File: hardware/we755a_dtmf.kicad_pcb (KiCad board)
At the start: 2 copper layers, 50.8 x 88.9 mm, 44 parts, among them J1 Conn_01x06_Male, J2 UPDI, J3 Conn_02x10_Odd_Even, U1 AVR128DA28-I/SS, U2 MT8870, U3 H11AA1, U4 LAA108, U5 LAA108, U6 LAA108, U7 LAA108, U8 LAA108, Y1 32.767KHz, Y2 3.579545MHZ

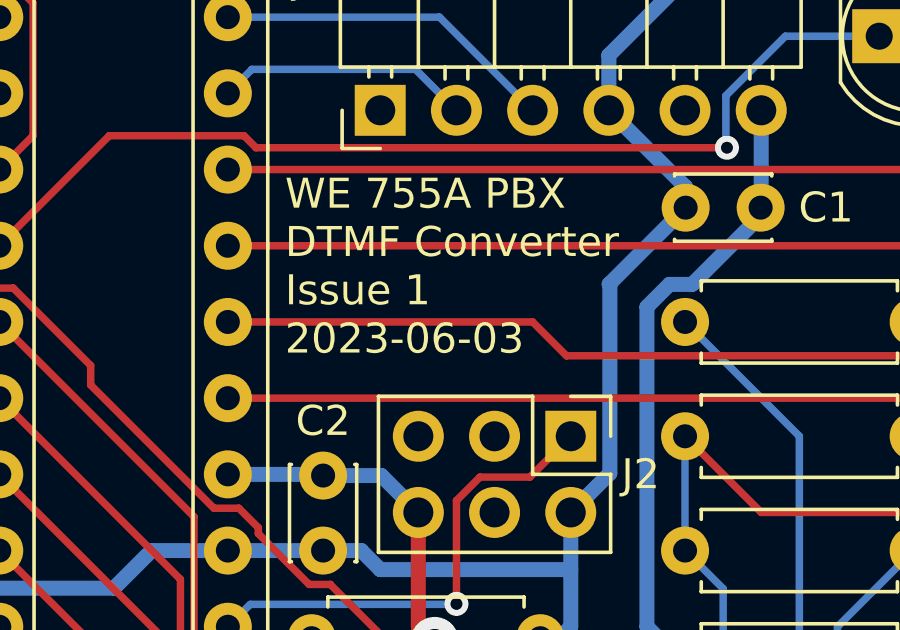
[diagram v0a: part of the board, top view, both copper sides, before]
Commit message: Update PCB to Rev2: No functional changes.
    * Rev 1 and Rev 2 PCBs are identical except for the silkscreen.
    * Rename LINK_B to LINK_E on schematic and layout.
    * Correct value of C1 on schematic.
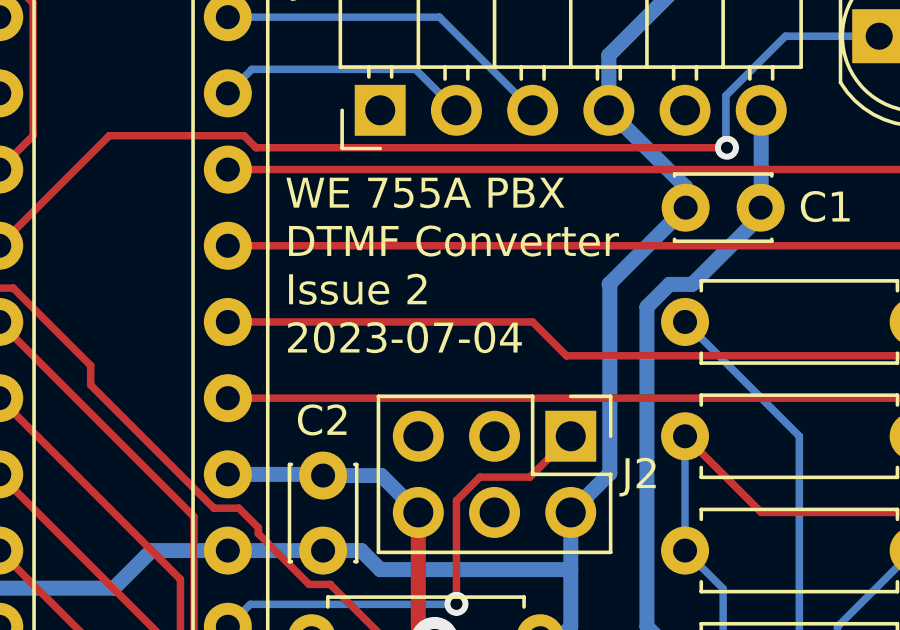
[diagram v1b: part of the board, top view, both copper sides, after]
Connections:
- net /LINK_B renamed /LINK_E
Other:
- board text added: "E"
- board text added: "WE 755A PBX DTMF Converter Issue 2 2023-07-04"
- board text added: "WE 755A PBX DTMF Converter github.com/hharte/we755a_dtmf Issue 2 - 2023-07-04"
- board text removed: "B"
- board text removed: "WE 755A PBX DTMF Converter Issue 1 2023-06-03"
- board text removed: "WE 755A PBX DTMF Converter github.com/hharte/we755a_dtmf Issue 1 - 2023-06-03"
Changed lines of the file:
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@@
   (title_block
     (title "WE 755A PBX DTMF Converter")
-    (date "2023-06-03")
-    (rev "1")
+    (date "2023-07-04")
+    (rev "2")
     (company "Howard M. Harte")
     (comment 1 "https://github.com/hharte/we755a_dtmf")
@@
   (net 24 "/WE755A_B0")
   (net 25 "GNDPWR")
-  (net 26 "/LINK_B")
+  (net 26 "/LINK_E")
   (net 27 "/LINK_T2")
   (net 28 "/LINK_T3")
@@
       (net 49 "Net-(R13-Pad2)") (pintype "passive"))
     (pad "2" thru_hole oval (at 0 2.54 270) (size 1.6 1.6) (drill 0.8) (layers "*.Cu" "*.Mask")
-      (net 26 "/LINK_B") (pintype "passive"))
+      (net 26 "/LINK_E") (pintype "passive"))
     (pad "3" thru_hole oval (at 0 5.08 270) (size 1.6 1.6) (drill 0.8) (layers "*.Cu" "*.Mask")
       (net 63 "unconnected-(U3-NC-Pad3)") (pinfunction "NC") (pintype "no_connect"))
@@
       (net 82 "unconnected-(J3-Pin_15-Pad15)") (pinfunction "Pin_15") (pintype "passive+no_connect"))
     (pad "16" thru_hole oval (at 2.54 17.78 270) (size 1.7 1.7) (drill 1) (layers "*.Cu" "*.Mask")
-      (net 26 "/LINK_B") (pinfunction "Pin_16") (pintype "passive"))
+      (net 26 "/LINK_E") (pinfunction "Pin_16") (pintype "passive"))
     (pad "17" thru_hole oval (at 0 20.32 270) (size 1.7 1.7) (drill 1) (layers "*.Cu" "*.Mask")
       (net 3 "/TIP") (pinfunction "Pin_17") (pintype "passive"))
@@
         (effects (font (size 1 1) (thickness 0.15)))
     )
-    (fp_text value "MountingHole" (at 0 3.7) (layer "F.Fab")
+    (fp_text value "MountingHole" (at 0 3.7) (layer "F.Fab") hide
         (effects (font (size 1 1) (thickness 0.15)))
     )
@@
     (effects (font (size 1 1) (thickness 0.15)) (justify left bottom mirror))
   )
-  (gr_text "WE 755A PBX DTMF Converter\ngithub.com/hharte/we755a_dtmf\nIssue 1 - 2023-06-03" (at 70.993 27.813) (layer "B.SilkS")
+  (gr_text "WE 755A PBX DTMF Converter\ngithub.com/hharte/we755a_dtmf\nIssue 2 - 2023-07-04" (at 70.993 27.813) (layer "B.SilkS")
     (effects (font (size 1 1) (thickness 0.15)) (justify left bottom mirror))
   )
-  (gr_text "B" (at 53.721 110.744) (layer "B.SilkS")
+  (gr_text "E" (at 53.721 110.744) (layer "B.SilkS")
     (effects (font (size 1 1) (thickness 0.15)) (justify left bottom mirror))
   )
@@
     (effects (font (size 1 1) (thickness 0.15)) (justify left bottom))
   )
-  (gr_text "WE 755A PBX\nDTMF Converter\nIssue 1\n2023-06-03" (at 47.625 41.783) (layer "F.SilkS")
+  (gr_text "WE 755A PBX\nDTMF Converter\nIssue 2\n2023-07-04" (at 47.625 41.783) (layer "F.SilkS")
     (effects (font (size 1 1) (thickness 0.15)) (justify left bottom))
   )
   (dimension (type aligned) (layer "Dwgs.User")
+    (pts (xy 36.195 108.585) (xy 36.195 111.76))
+    (height 5.461)
+    (gr_text "3.1750 mm" (at 30.6324 116.5352 90) (layer "Dwgs.User")
+      (effects (font (size 1 1) (thickness 0.15)))
+    )
+    (format (prefix "") (suffix "") (units 3) (units_format 1) (precision 4))
+    (style (thickness 0.12) (arrow_length 1.27) (text_position_mode 2) (extension_height 0.58642) (extension_offset 0.5) keep_text_aligned)
+  )
+  (dimension (type aligned) (layer "Dwgs.User")
+    (pts (xy 36.195 108.585) (xy 80.645 108.585))
+    (height 8.763)
+    (gr_text "44.4500 mm" (at 58.42 116.198) (layer "Dwgs.User")
+      (effects (font (size 1 1) (thickness 0.15)))
+    )
+    (format (prefix "") (suffix "") (units 3) (units_format 1) (precision 4))
+    (style (thickness 0.12) (arrow_length 1.27) (text_position_mode 0) (extension_height 0.58642) (extension_offset 0.5) keep_text_aligned)
+  )
+  (dimension (type aligned) (layer "Dwgs.User")
     (pts (xy 32.385 22.86) (xy 32.385 111.76))
-    (height 1.905)
-    (gr_text "88.9000 mm" (at 29.33 67.31 90) (layer "Dwgs.User")
+    (height 5.1054)
+    (gr_text "88.9000 mm" (at 28.194 67.31 90) (layer "Dwgs.User")
       (effects (font (size 1 1) (thickness 0.15)))
     )
     (format (prefix "") (suffix "") (units 2) (units_format 1) (precision 4))
-    (style (thickness 0.15) (arrow_length 1.27) (text_position_mode 0) (extension_height 0.58642) (extension_offset 0) keep_text_aligned)
+    (style (thickness 0.15) (arrow_length 1.27) (text_position_mode 2) (extension_height 0.58642) (extension_offset 0) keep_text_aligned)
   )
   (dimension (type aligned) (layer "Dwgs.User")
@@
     (style (thickness 0.15) (arrow_length 1.27) (text_position_mode 0) (extension_height 0.58642) (extension_offset 0) keep_text_aligned)
   )
+  (dimension (type aligned) (layer "Dwgs.User")
+    (pts (xy 36.195 108.585) (xy 33.02 108.585))
+    (height -6.8326)
+    (gr_text "3.1750 mm" (at 41.0464 115.5192) (layer "Dwgs.User")
+      (effects (font (size 1 1) (thickness 0.15)))
+    )
+    (format (prefix "") (suffix "") (units 3) (units_format 1) (precision 4))
+    (style (thickness 0.12) (arrow_length 1.27) (text_position_mode 2) (extension_height 0.58642) (extension_offset 0.5) keep_text_aligned)
+  )
   (segment (start 45.4828 76.4772) (end 50.8 71.16) (width 0.5) (layer "F.Cu") (net 1))

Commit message: Update to KiCAD 8.0.1.
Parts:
- C1: value 1uF -> 0.1uF

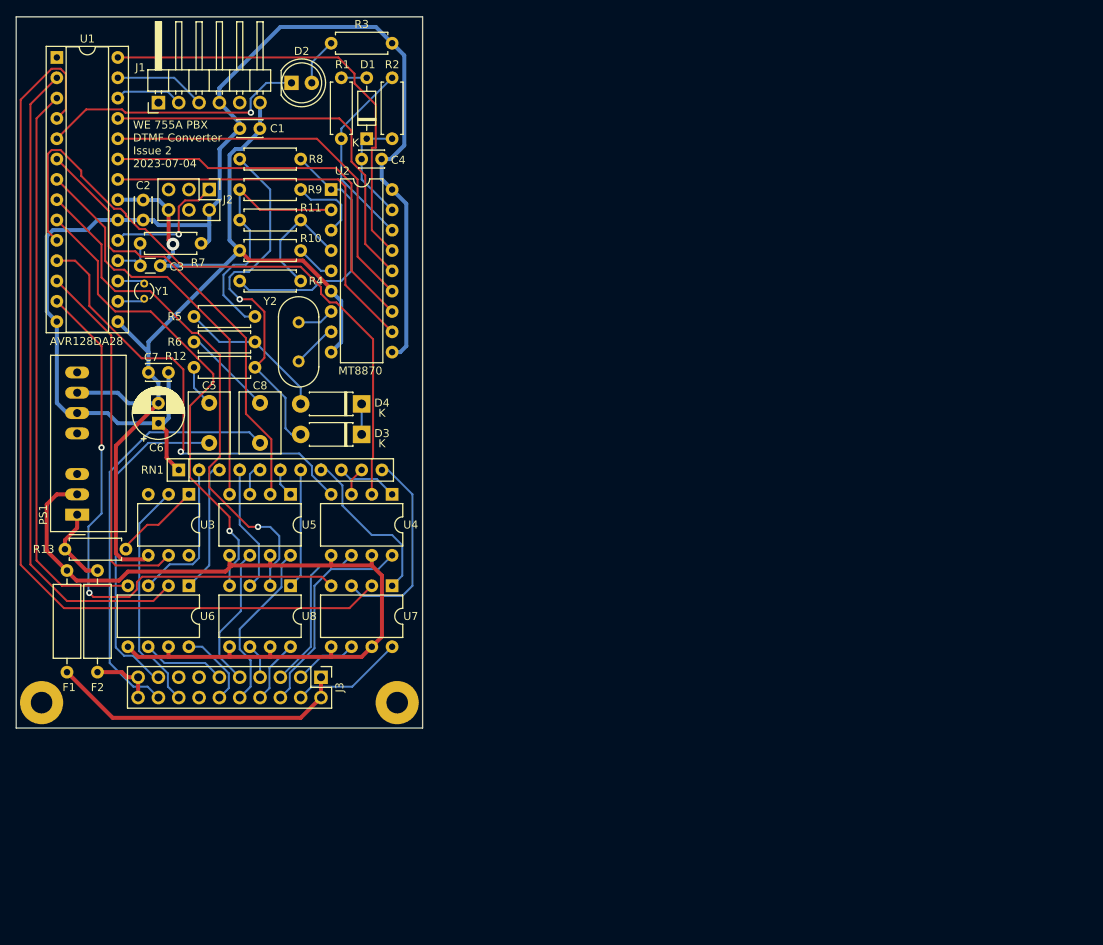
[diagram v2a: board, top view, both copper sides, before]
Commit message: Issue 3: Smaller board.     * Smaller board.     * Jumper options for DTMF converter and station concentrator.
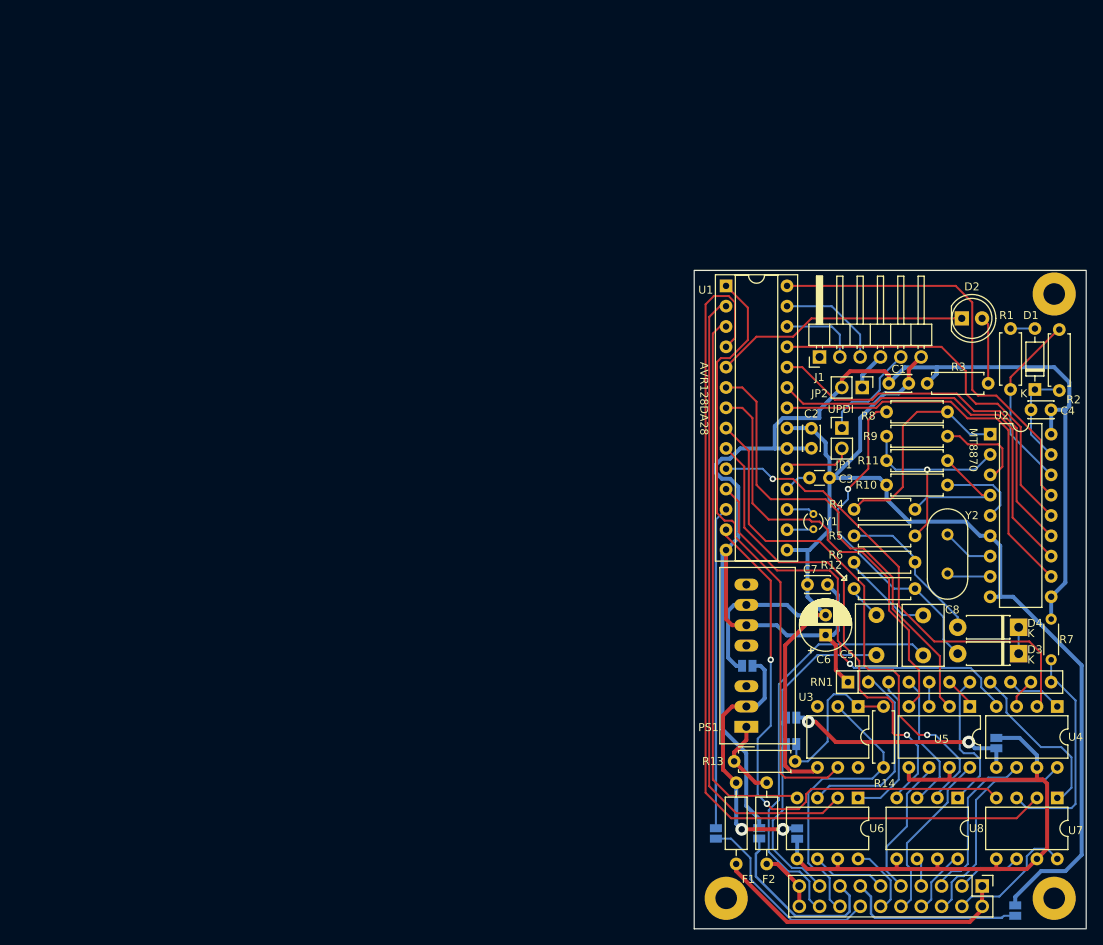
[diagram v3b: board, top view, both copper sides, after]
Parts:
- removed H1, H2: MountingHole, MountingHole:MountingHole_2.7mm_Pad
- removed J2: UPDI, Connector_PinHeader_2.54mm:PinHeader_2x03_P2.54mm_Vertical
- added JP1: Jumper_2_Open, Connector_PinHeader_2.54mm:PinHeader_1x02_P2.54mm_Vertical, F.Cu at (136.2, 74.3)
- added JP10: 5V_J3, Jumper:SolderJumper-2_P1.3mm_Open_Pad1.0x1.5mm, B.Cu at (120.5, 124.9)
- added JP2: Jumper_2_Open, Connector_PinHeader_2.54mm:PinHeader_1x02_P2.54mm_Vertical, F.Cu at (138.8, 69.2)
- added JP3: GRD_TIE, Jumper:SolderJumper-2_P1.3mm_Open_Pad1.0x1.5mm, B.Cu at (124.4, 104.0)
- added JP4: LINK6_G_SSR, Jumper:SolderJumper-2_P1.3mm_Open_Pad1.0x1.5mm, B.Cu at (155.5, 113.6)
- added JP5: G_SSR_GNDPWR, Jumper:SolderJumper-2_P1.3mm_Open_Pad1.0x1.5mm, B.Cu at (130.6, 125.0)
- added JP6: TIP_IN, Jumper:SolderJumper-2_P1.3mm_Open_Pad1.0x1.5mm, B.Cu at (129.9, 113.8)
- added JP7: LINK6_TIP, Jumper:SolderJumper-2_P1.3mm_Open_Pad1.0x1.5mm, B.Cu at (129.9, 110.5)
- added JP8: GND_J3, Jumper:SolderJumper-2_P1.3mm_Open_Pad1.0x1.5mm, B.Cu at (157.9, 134.6)
- added JP9: 5V_J3, Jumper:SolderJumper-2_P1.3mm_Open_Pad1.0x1.5mm, B.Cu at (125.9, 124.9)
- added R14: 120, Resistor_THT:R_Axial_DIN0207_L6.3mm_D2.5mm_P7.62mm_Horizontal, F.Cu at (141.4, 116.7)
- F1, F2: footprint Resistor_THT:R_Axial_DIN0309_L9.0mm_D3.2mm_P12.70mm_Horizontal -> Resistor_THT:R_Axial_DIN0207_L6.3mm_D2.5mm_P10.16mm_Horizontal
- J3: footprint Connector_PinHeader_2.54mm:PinHeader_2x10_P2.54mm_Vertical -> ac125a_dtmf:WE755A-DTMF
- PS1: value SPBW06 -> SPBW06-5
- R7: value 4.7K -> 220; footprint Resistor_THT:R_Axial_DIN0207_L6.3mm_D2.5mm_P7.62mm_Horizontal -> Resistor_THT:R_Axial_DIN0204_L3.6mm_D1.6mm_P5.08mm_Horizontal
- RN1: value R_Network10_US -> R_Network10_220R
- moved R7 116.2 mm to (162.4, 98.1), turned to -90 degrees
- moved R3 92.5 mm to (154.5, 68.7), turned to 180 degrees
- moved C4 89.3 mm to (159.9, 72.0)
- moved R1 89.3 mm to (157.3, 61.8)
- moved D1 89.2 mm to (160.4, 69.4)
- moved R2 89.1 mm to (163.4, 69.6)
- moved U5 89.0 mm to (152.2, 109.1)
- moved D2 88.8 mm to (151.2, 60.6)
- moved J1 88.5 mm to (133.4, 65.4)
- moved Y1 88.5 mm to (132.7, 85.0)
- moved U1 88.4 mm to (121.8, 56.5)
- moved C2 88.3 mm to (132.4, 76.8)
- moved U2 87.9 mm to (154.8, 75.0)
- moved RN1 87.8 mm to (137.0, 106.0)
- moved R13 87.8 mm to (122.8, 115.9)
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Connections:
- J1 pad 4: +5V -> Net-(J1-Pin_4)
- J1 pad 5: unconnected-(J1-Pin_5-Pad5) -> /UPDI_EXT
- J3 pad 13: unconnected-(J3-Pin_13-Pad13) -> /GND_J3
- J3 pad 14: unconnected-(J3-Pin_14-Pad14) -> /PD6_J3
- J3 pad 15: unconnected-(J3-Pin_15-Pad15) -> /5V_J3
- R7 pad 2: /RESET# -> Net-(RN1-R10)
- U1 pad 1: unconnected-(U1-PA7-Pad1) -> /~{LINK_ACTIVE}
- U1 pad 12: /~{LINK_ACTIVE} -> /PD6
- U4 pad 5: GNDPWR -> Net-(JP4-A)
- U4 pad 7: GNDPWR -> /G_SSR
- U5 pad 5: GNDPWR -> /G_SSR
- U5 pad 7: GNDPWR -> /G_SSR
- U6 pad 5: GNDPWR -> /G_SSR
- U6 pad 7: GNDPWR -> /G_SSR
- U7 pad 5: GNDPWR -> /G_SSR
- U7 pad 7: GNDPWR -> /G_SSR
- U8 pad 5: GNDPWR -> /G_SSR
- U8 pad 7: GNDPWR -> /G_SSR
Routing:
- net /G_SSR: track 0.00 -> 79.9 mm
- net GNDPWR: track 106.3 -> 33.6 mm, vias 0 -> 2
- net GND: track 132.2 -> 183.0 mm, vias 1 -> 0
- net /PD6: track 0.00 -> 40.4 mm
- net /~{LINK_ACTIVE}: track 45.7 -> 76.1 mm
- net Net-(JP4-A): track 0.00 -> 29.0 mm, vias 0 -> 2
- net /PD6_J3: track 0.00 -> 24.4 mm
- net /~{D5-6}: track 82.4 -> 58.7 mm, vias 0 -> 1
- net /5V_J3: track 0.00 -> 22.5 mm
- net /GND_J3: track 0.00 -> 22.4 mm
- net +5V: track 162.8 -> 184.6 mm
- net /UPDI_EXT: track 0.00 -> 13.1 mm
- net Net-(JP6-A): track 10.4 -> 20.0 mm
- net /LINK_E: track 29.4 -> 37.4 mm
- net /UPDI: track 16.1 -> 8.62 mm, vias 1 -> 0
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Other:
- board size 50.8 x 88.9 mm -> 49 x 82.3 mm
- board text added: "755A Concentrator: Open JP4, JP5, Remove R13. Short JP6, JP7, Install R14."
- board text added: "755A DTMF: Short JP4, JP5, Install R13. Open JP6, JP7, Remove R14."
- board text added: "JP3: Open - Isolate GRD"
- board text added: "PD6"
- board text added: "SP"
- board text added: "UP DI"
- board text added: "WE 755A PBX DTMF Converter Issue 3 2024-04-07"
- board text removed: "WE 755A PBX DTMF Converter Issue 2 2023-07-04"
- board text removed: "WE 755A PBX DTMF Converter github.com/hharte/we755a_dtmf Issue 2 - 2023-07-04"

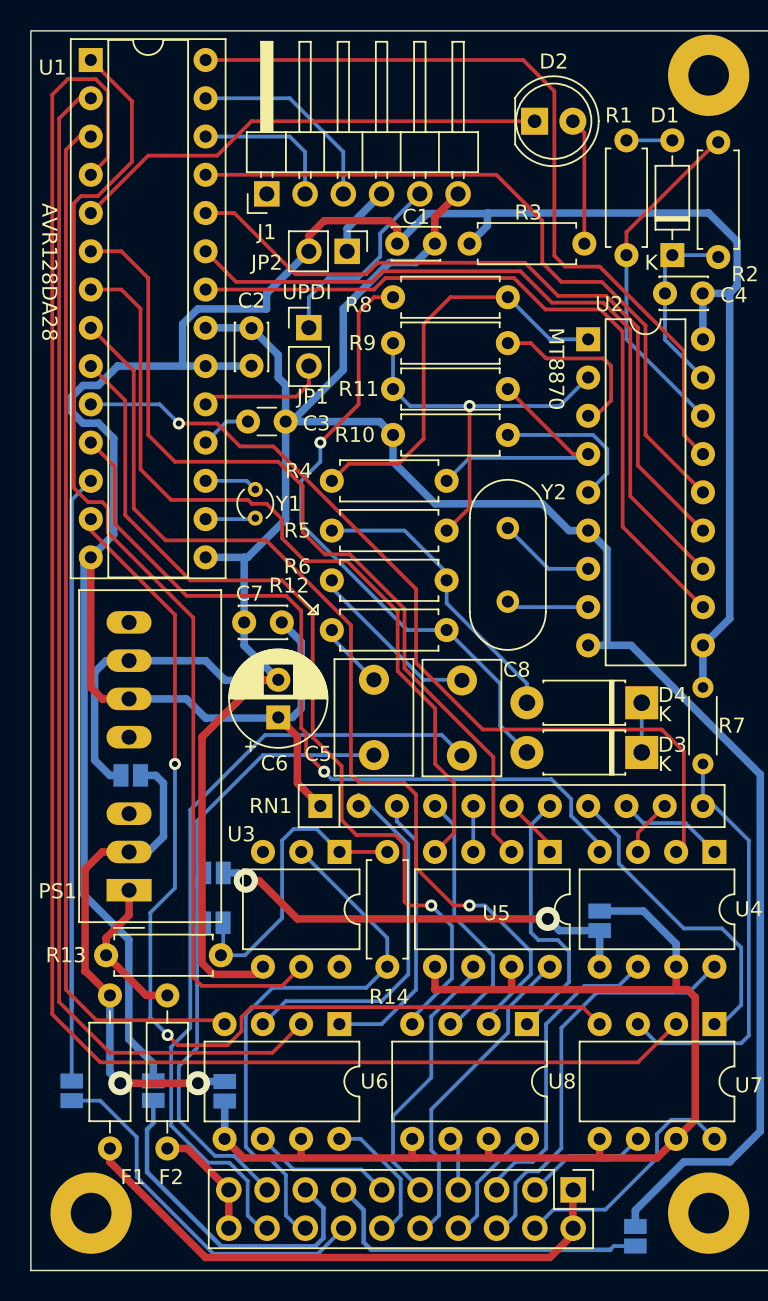
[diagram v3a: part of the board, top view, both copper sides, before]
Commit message: Issue 4: Change fuses to PTCs.
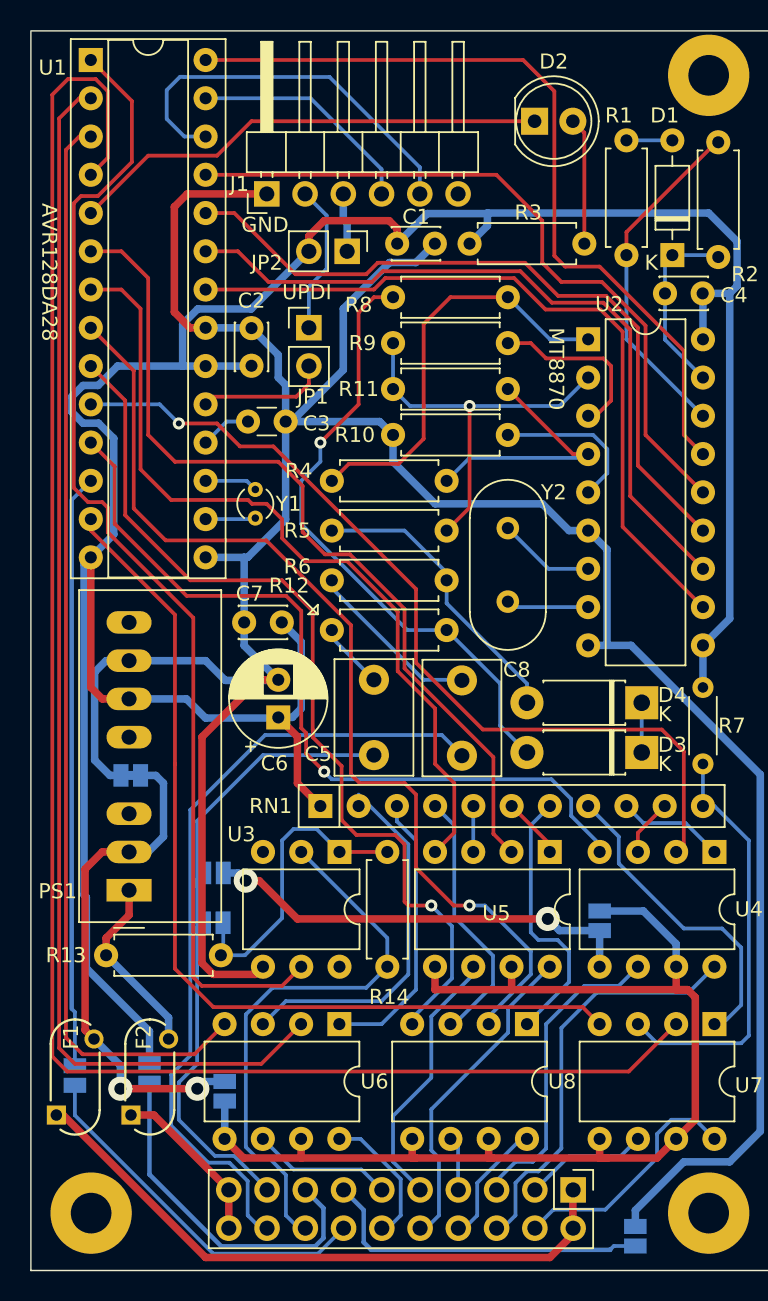
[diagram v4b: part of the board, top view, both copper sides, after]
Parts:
- F1, F2: value Fuse 630mA -> Polyfuse; footprint Resistor_THT:R_Axial_DIN0207_L6.3mm_D2.5mm_P10.16mm_Horizontal -> ac125a_dtmf:FUSE_RXEF025_LTF
- JP3: footprint Jumper:SolderJumper-2_P1.3mm_Open_Pad1.0x1.5mm -> Jumper:SolderJumper-2_P1.3mm_Bridged_Pad1.0x1.5mm
- moved F1 5.89 mm to (120.7, 124.0), turned to 90 degrees
- moved F2 5.54 mm to (125.7, 124.0), turned to 90 degrees
- moved JP9 1.17 mm to (125.6, 123.8)
- moved JP10 1.04 mm to (120.7, 123.9)
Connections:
- F1 pad 1: GNDPWR -> /WE755A_G0
- F1 pad 2: /WE755A_G0 -> GNDPWR
- F2 pad 1: -BATT -> /WE755A_B0
- F2 pad 2: /WE755A_B0 -> -BATT
- J1 pad 1: unconnected-(J1-Pin_1-Pad1) -> GND
- J1 pad 2: /TXD -> /UPDI_EXT
- J1 pad 3: /RXD -> Net-(J1-Pin_3)
- J1 pad 4: Net-(J1-Pin_4) -> /RXD
- J1 pad 5: /UPDI_EXT -> /TXD
- J1 pad 6: GND -> unconnected-(J1-Pin_6-Pad6)
- JP2 pad 1: Net-(J1-Pin_4) -> Net-(J1-Pin_3)
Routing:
- net /TXD: track 9.82 -> 26.4 mm
- net GND: track 183.0 -> 195.0 mm
- net /~{R_SPARE}: track 68.7 -> 61.9 mm, vias 2 -> 0
- net Net-(J1-Pin_4): track 4.76 -> 0.00 mm
- net /WE755A_G0: track 37.4 -> 41.4 mm
- net Net-(J1-Pin_3): track 0.00 -> 3.92 mm
- net /~{T3}: track 69.3 -> 72.8 mm
- net /WE755A_B0: track 7.76 -> 11.1 mm
- net /UPDI_EXT: track 13.1 -> 9.97 mm
- net /~{T2}: track 79.6 -> 82.0 mm
- net /~{C1}: track 115.3 -> 117.5 mm
- net -BATT: track 10.1 -> 12.2 mm
- net /RXD: track 13.4 -> 15.3 mm
- net +5V: track 184.6 -> 182.7 mm
- net /5V_J3: track 22.5 -> 23.5 mm
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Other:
- board text added: "JP3: Cut - Isolate GRD"
- board text added: "NC"
- board text added: "WE 755A PBX DTMF Converter Issue 4 2024-05-27"
- board text removed: "JP3: Open - Isolate GRD"
- board text removed: "WE 755A PBX DTMF Converter Issue 3 2024-04-07"
